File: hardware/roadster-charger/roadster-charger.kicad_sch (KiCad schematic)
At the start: 51 parts, among them J1 USB4505-03-0-A_REVA, J2 USB4505-03-0-A_REVA, J3 54-00166, Q1 CSD19532Q5B, U1 FUSB307BMPX, U10 OPA340NA, U2 ESP32-C3-MINI-1, U3 INA168, U4 LM5050-1, U5 INA168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

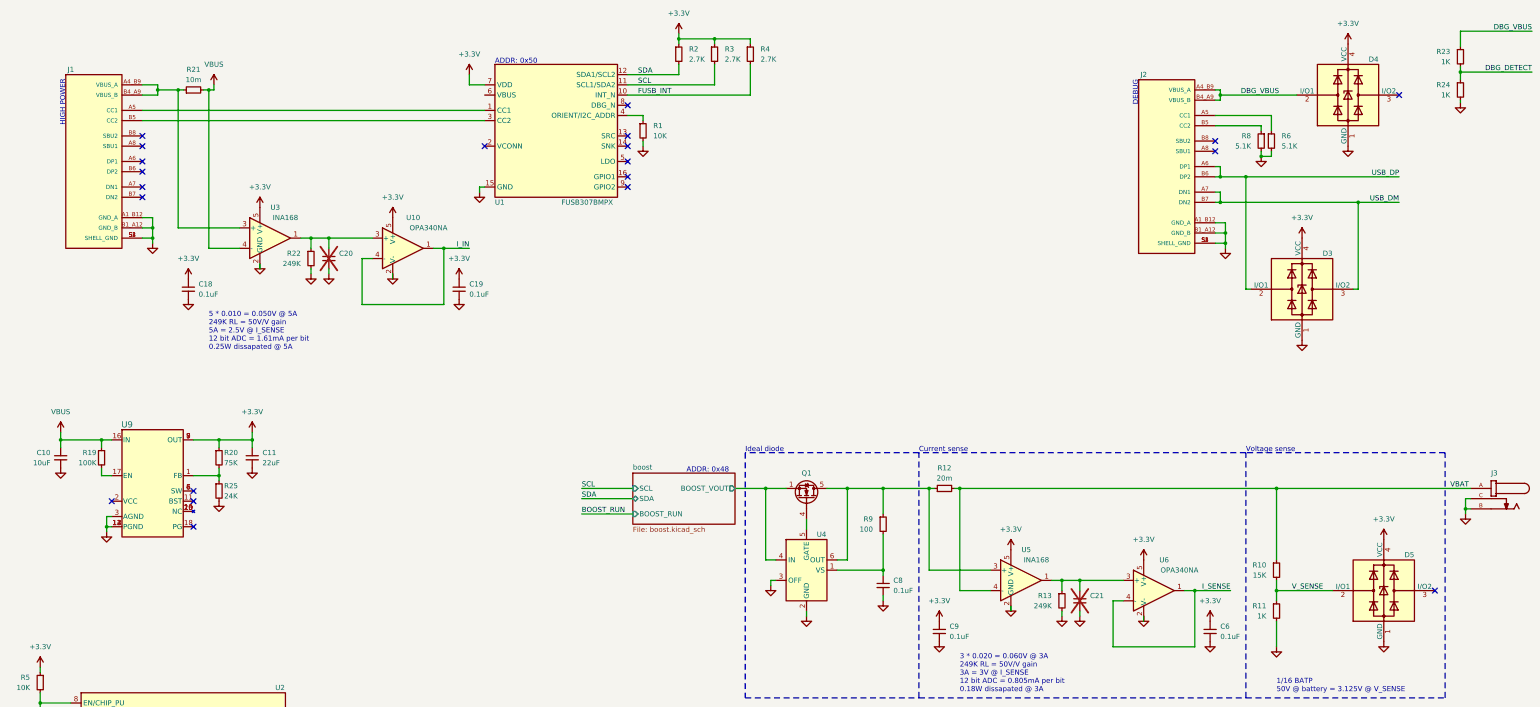
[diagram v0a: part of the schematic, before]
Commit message: fix accidental schem. grid change, add footprints and MPNs
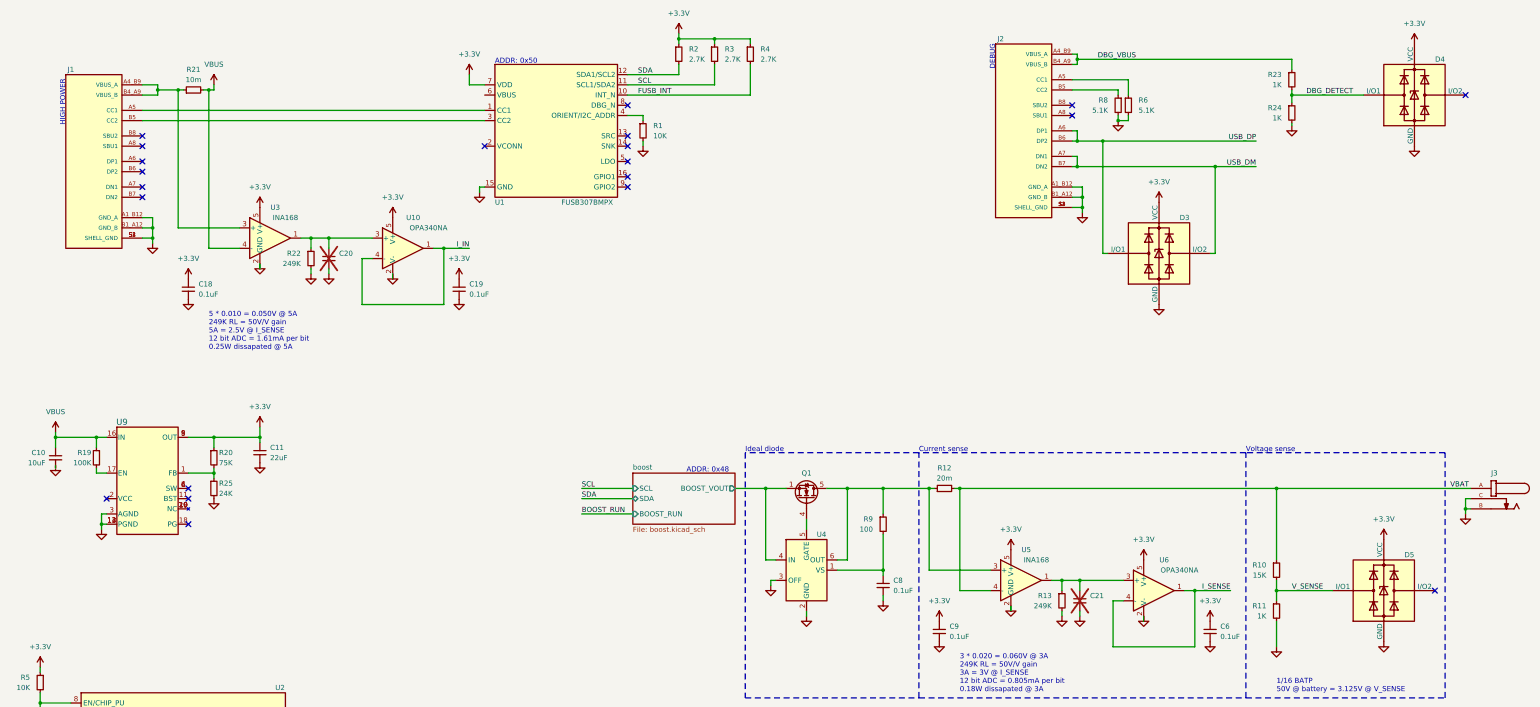
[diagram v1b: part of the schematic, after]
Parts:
- C1, C10: footprint (none) -> Capacitor_SMD:C_1206_3216Metric; MPN (none) -> CL31A106MBHNNNE
- C11: footprint (none) -> Capacitor_SMD:C_1206_3216Metric; MPN (none) -> CL31A226KAHNNNE
- C18, C19, C3, C4, C5, C6, C9: footprint (none) -> Capacitor_SMD:C_0603_1608Metric; MPN (none) -> CL10B104KB8NNNC
- C2: footprint (none) -> Capacitor_SMD:C_0805_2012Metric; MPN (none) -> CL21B105KAFNNNE
- C20, C21: footprint (none) -> Capacitor_SMD:C_0603_1608Metric; MPN (none) -> DNP
- C8: footprint (none) -> Capacitor_SMD:C_0603_1608Metric; MPN (none) -> CL10B104KC8NNNC
- D1, D2: MPN (none) -> COM-16347
- D3, D4, D5: MPN (none) -> PRTR5V0U2X,215
- J1, J2: value USB4505-03-0-A_REVA -> USB4505-03-0-A; footprint GCT_USB4505-03-0-A_REVA -> USB4505-03-0-A_REVA:GCT_USB4505-03-0-A_REVA; MANUFACTURER GCT -> (none); MAXIMUM_PACKAGE_HEIGHT 2.46mm -> (none); MPN (none) -> USB4505-03-0-A; PARTREV A -> (none); STANDARD Manufacturer Recommendations -> (none)
- J3: Availability In Stock -> (none); Check_prices https://www.snapeda.com/parts/54-00166/Tensility+Internatio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 -> (none); MANUFACTURER TENSILITY -> (none); MAXIMUM_PACKAGE_HEIGHT 11.2mm -> (none); MF Tensility International Corp -> (none); MP 54-00166 -> (none); MPN (none) -> 54-00166; PARTREV A -> (none); Purchase-URL https://www.snapeda.com/api/url_track_click_mouser/?unipart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 -> (none); SNAPEDA_PN 54-00166 -> (none); STANDARD Manufacturer Recommendations -> (none); SnapEDA_Link https://www.snapeda.com/parts/54-00166/Tensility+Internatio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 -> (none)
- Q1: MPN (none) -> CSD19532Q5B
- R1, R5, R7: footprint (none) -> Resistor_SMD:R_0603_1608Metric; MPN (none) -> RMCF0603FT10K0
- R10: footprint (none) -> Resistor_SMD:R_0603_1608Metric; MPN (none) -> RC0603JR-0715KL
- R11, R23, R24: footprint (none) -> Resistor_SMD:R_0603_1608Metric; MPN (none) -> RC0603FR-071KL
- R12: footprint (none) -> Resistor_SMD:R_0603_1608Metric
- R13, R22: footprint (none) -> Resistor_SMD:R_0603_1608Metric; MPN (none) -> RMCF0603FT249K
- R19: footprint (none) -> Resistor_SMD:R_0603_1608Metric; MPN (none) -> RC0603FR-07100KL
- R2, R3, R4: footprint (none) -> Resistor_SMD:R_0603_1608Metric; MPN (none) -> RC0603JR-072K7L
- R20: footprint (none) -> Resistor_SMD:R_0603_1608Metric; MPN (none) -> RC0603FR-0775KL
- R21: footprint (none) -> Resistor_SMD:R_0603_1608Metric; MPN LVT06R0020HER -> LVT06R0100FER
- R25: footprint (none) -> Resistor_SMD:R_0603_1608Metric; MPN (none) -> RC0603FR-1024KL
- R6, R8: footprint (none) -> Resistor_SMD:R_0603_1608Metric; MPN (none) -> RC0603FR-075K1L
- R9: footprint (none) -> Resistor_SMD:R_0603_1608Metric; MPN (none) -> RMCF0603FT100R
- U1: MPN (none) -> FUSB307BMPX
- U10, U6: MPN (none) -> OPA340NA
- U2: footprint Espressif:ESP32-C3-MINI-1 -> PCM_Espressif:ESP32-C3-MINI-1; MPN (none) -> ESP32-C3-MINI-1-N4
- U3, U5: MPN (none) -> INA168NA
- U4: MPN (none) -> LM5050MKX-1/NOPB
- U9: footprint QFN3p0x5p0x1p6_MPM3606A_MNP -> MPM3606A:QFN3p0x5p0x1p6_MPM3606A_MNP; MPN (none) -> MPM3606AGQV-P
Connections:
- net DBG_DETECT: now also D4.2 (I/O1)
- net DBG_VBUS: no longer D4.2 (I/O1)
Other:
- moved on the sheet: C10, C11, J2, R19, R20, R23, R24, R25, R6, R8, U9

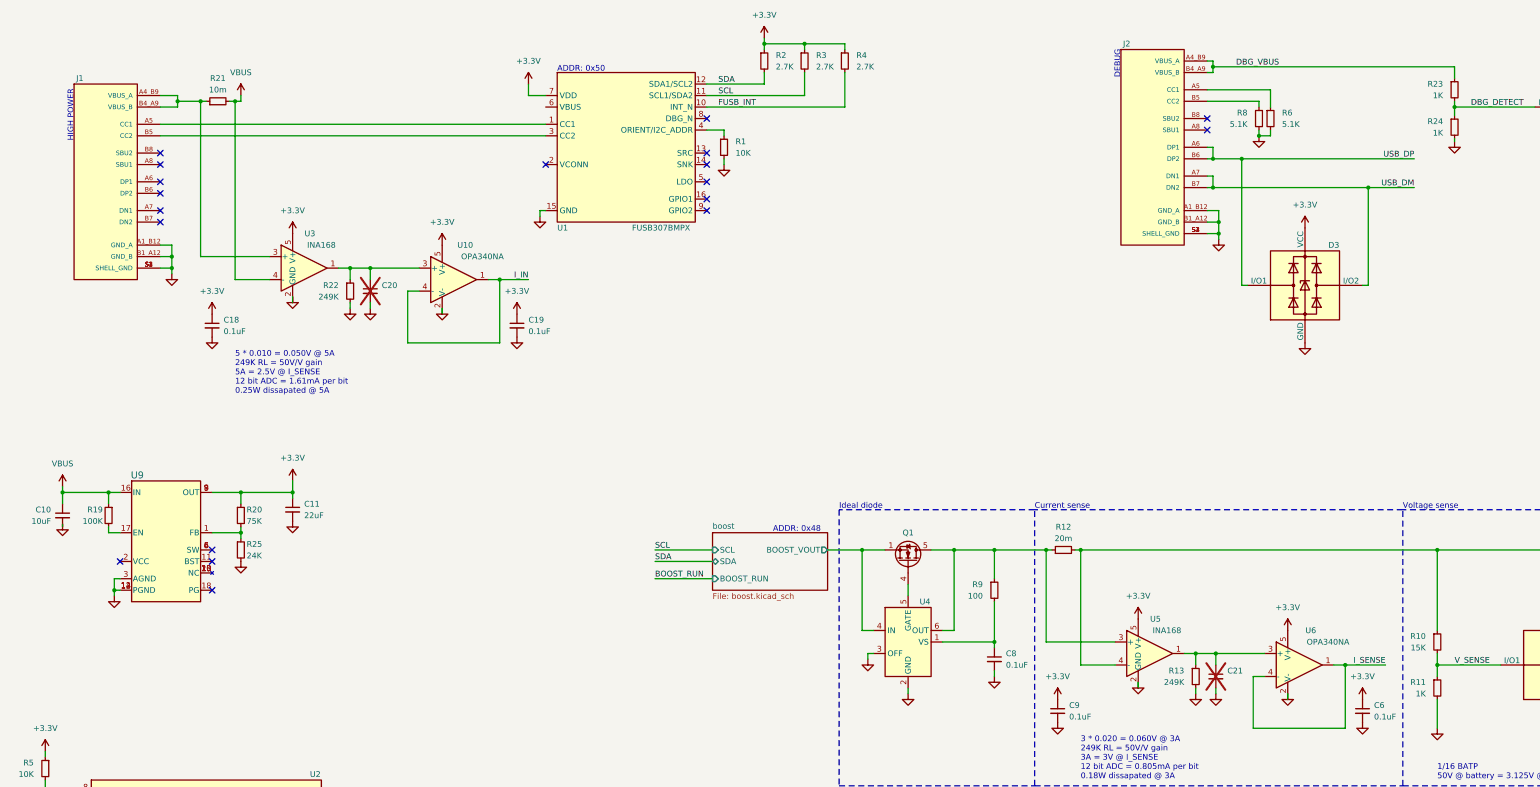
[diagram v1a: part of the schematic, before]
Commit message: edit ERC rules, clean up ERC errors, cleanup more off grid parts
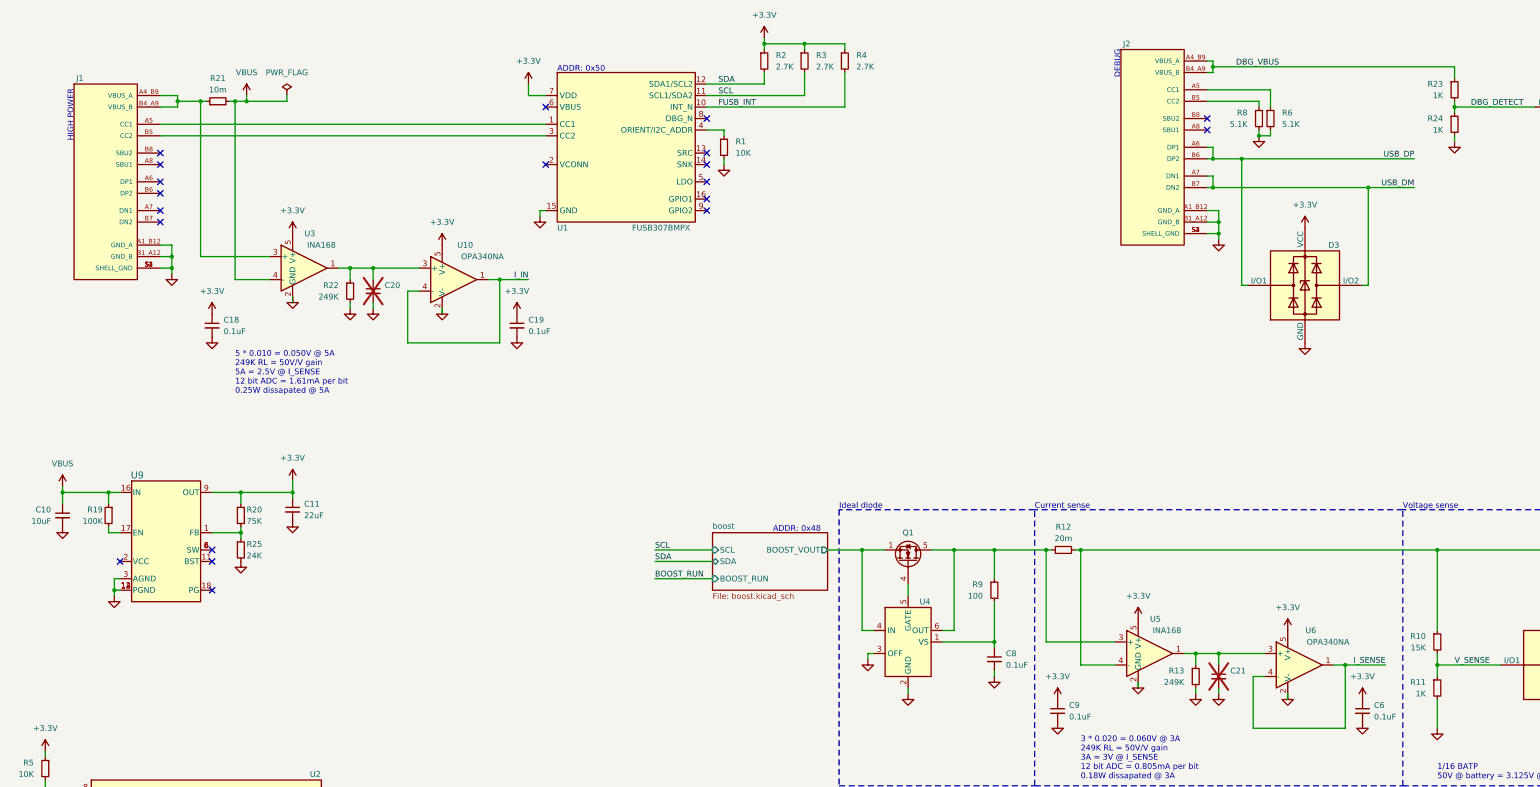
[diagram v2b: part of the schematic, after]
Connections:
- now unconnected: U9.10 (NC), U9.15 (NC), U9.19 (NC), U9.20 (NC)
- no-connect marks 24 -> 25
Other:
- moved on the sheet: C20, C21, R24

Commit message: wip routing
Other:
- note added: "CHANGE FB RESISTOR VALUES"
- note added: "TVS CLAMP"
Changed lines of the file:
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@@
     (effects (font (size 1.27 1.27)) (justify left bottom))
+  )
+  (text "TVS CLAMP" (at 210.82 181.61 0)
+    (effects (font (size 3 3) (thickness 0.6) bold (color 255 22 22 1)) (justify left bottom))
   )
   (text "1/16 BATP\n50V @ battery = 3.125V @ V_SENSE" (at 340.36 189.23 0)
@@
     (effects (font (size 1.27 1.27)) (justify left bottom))
   )
+  (text "CHANGE FB RESISTOR VALUES" (at 31.75 158.75 0)
+    (effects (font (size 3 3) (thickness 0.6) bold (color 255 22 22 1)) (justify left bottom))
+  )
   (label "V_SENSE" (at 344.17 163.83 0) (fields_autoplaced)

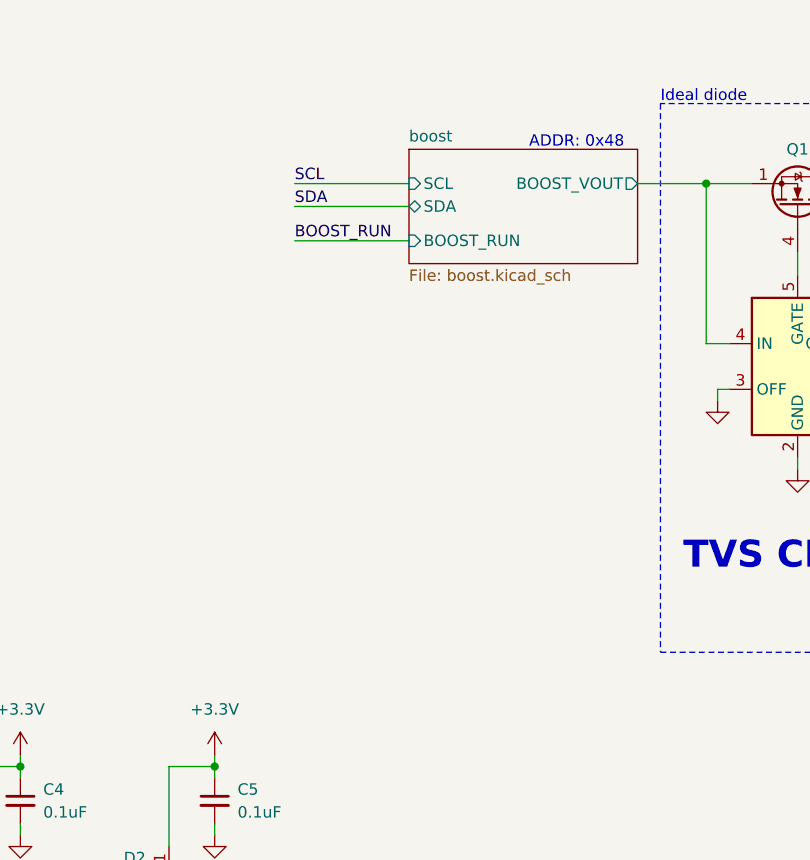
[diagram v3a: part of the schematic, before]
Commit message: add LM75 i2c current sensor
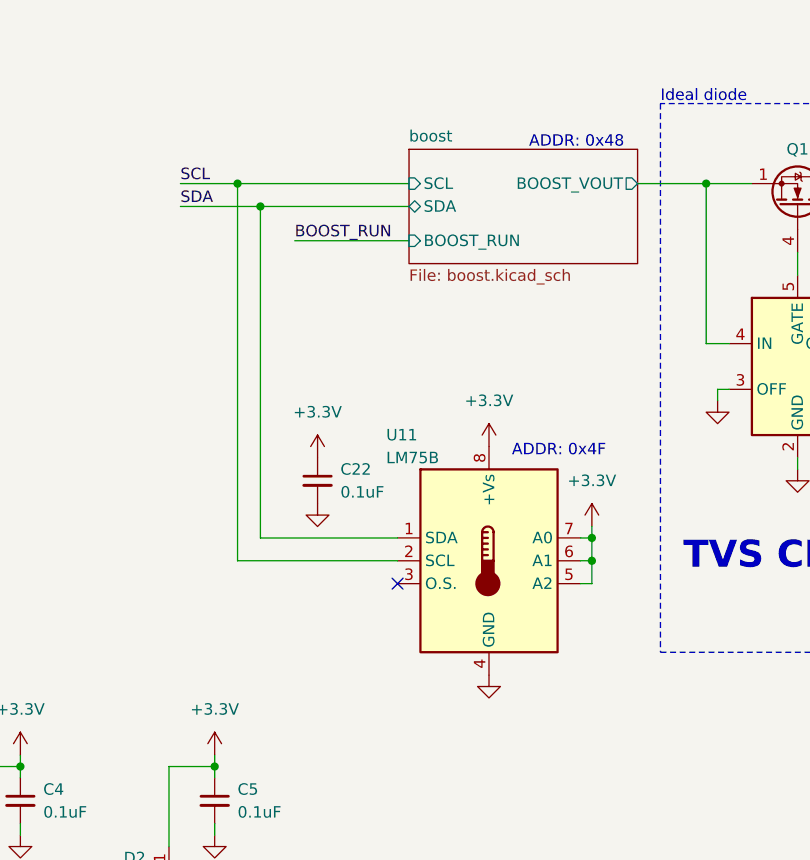
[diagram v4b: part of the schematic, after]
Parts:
- added C22: 0.1uF, Capacitor_SMD:C_0603_1608Metric, symbol Device:C_Small
- added U11: LM75B, Package_SO:SOIC-8_3.9x4.9mm_P1.27mm, symbol Sensor_Temperature:LM75B
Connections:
- net +3.3V: now also C22.1, U11.5 (A2), U11.6 (A1), U11.7 (A0), U11.8 (+Vs)
- net GND: now also C22.2, U11.4 (GND)
- net SCL: now also U11.2 (SCL)
- net SDA: now also U11.1 (SDA)
- no-connect marks 25 -> 26
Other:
- note added: "ADDR: 0x4F"

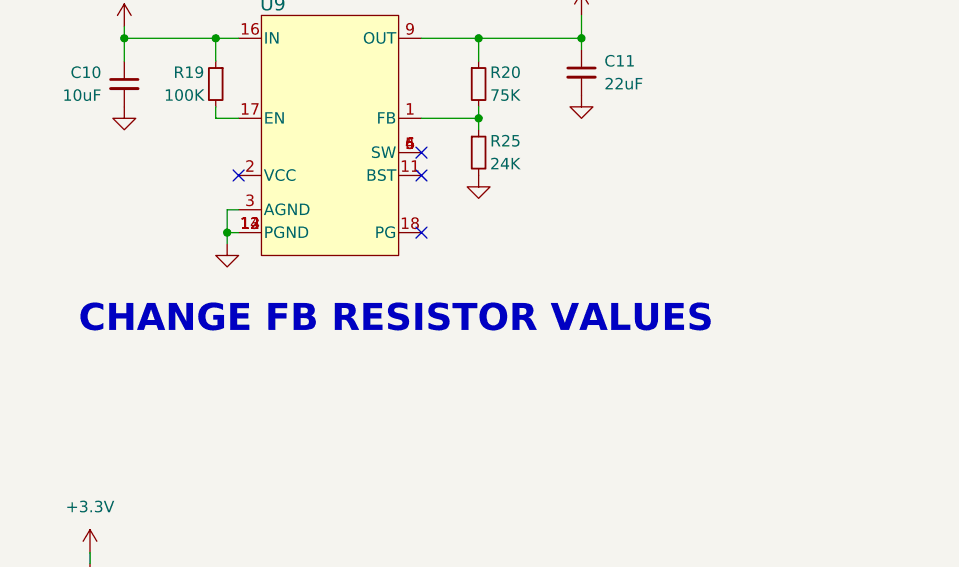
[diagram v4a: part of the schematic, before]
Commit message: add AAM resistor to 3V3 regulator, validate feedback resistors
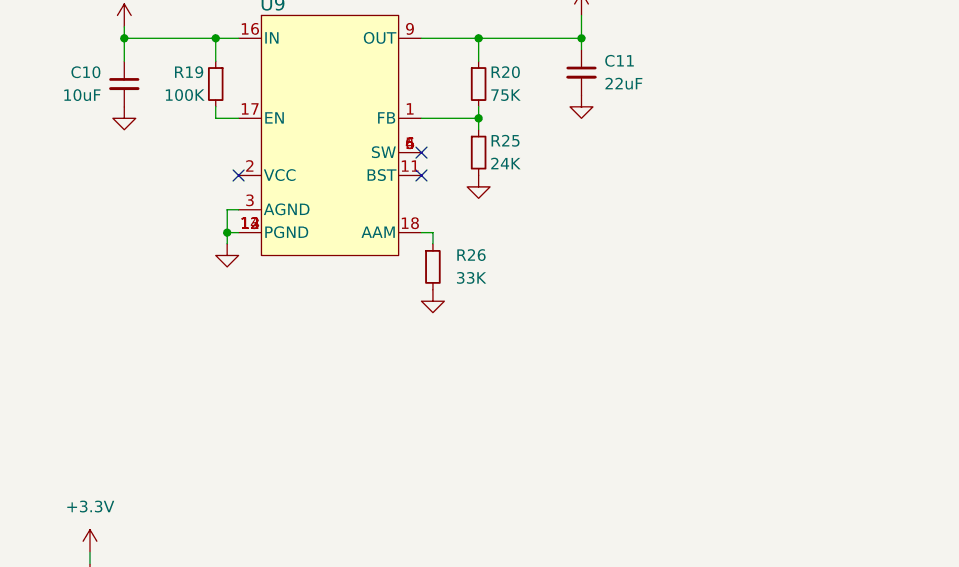
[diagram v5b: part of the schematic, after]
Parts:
- added R26: 33K, Resistor_SMD:R_0603_1608Metric, symbol Device:R_Small
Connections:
- net GND: now also R26.2
- net at U9.18 (AAM): now also R26.1
- no-connect marks 26 -> 25
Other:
- note removed: "CHANGE FB RESISTOR VALUES"
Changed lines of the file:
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@@
   (no_connect (at 289.56 43.18))
   (no_connect (at 69.85 140.97))
-  (no_connect (at 69.85 147.32))
   (no_connect (at 289.56 45.72))
   (no_connect (at 161.29 219.71))
@@
     (stroke (width 0) (type default))
   )
+  (wire (pts (xy 69.85 147.32) (xy 71.12 147.32))
+    (stroke (width 0) (type default))
+  )
   (polyline (pts (xy 208.28 190.5) (xy 251.46 190.5))
     (stroke (width 0) (type dash))
@@
     (stroke (width 0) (type default))
   )
+  (wire (pts (xy 71.12 147.32) (xy 71.12 148.59))
+    (stroke (width 0) (type default))
+  )
   (wire (pts (xy 96.52 207.01) (xy 109.22 207.01))
     (stroke (width 0) (type default))
@@
     (effects (font (size 1.27 1.27)) (justify left bottom))
   )
-  (text "CHANGE FB RESISTOR VALUES" (at 31.75 158.75 0)
-    (effects (font (size 3 3) (thickness 0.6) bold (color 255 22 22 1)) (justify left bottom))
-  )
   (label "V_SENSE" (at 344.17 163.83 0) (fields_autoplaced)
     (effects (font (size 1.27 1.27)) (justify left bottom))
@@
     )
   )
+  (symbol (lib_id "Device:R_Small") (at 71.12 151.13 0) (unit 1)
+    (in_bom yes) (on_board yes) (dnp no)
+    (property "Reference" "R26" (at 73.66 149.86 0)
+      (effects (font (size 1.27 1.27)) (justify left))
+    )
+    (property "Value" "33K" (at 73.66 152.4 0)
+      (effects (font (size 1.27 1.27)) (justify left))
+    )
+    (property "Footprint" "Resistor_SMD:R_0603_1608Metric" (at 71.12 151.13 0)
+      (effects (font (size 1.27 1.27)) hide)
+    )
+    (property "Datasheet" "~" (at 71.12 151.13 0)
+      (effects (font (size 1.27 1.27)) hide)
+    )
+    (property "MPN" "RMCF0603FT33K0" (at 71.12 151.13 0)
+      (effects (font (size 1.27 1.27)) hide)
+    )
+    (pin "1")
+    (pin "2")
+    (instances
+      (project "roadster-charger"
+        (path "/57ecac41-cd8a-4182-a81e-fed3e381aedd"
+          (reference "R26") (unit 1)
+        )
+      )
+    )
+  )
   (symbol (lib_id "power:GND") (at 182.88 53.34 0) (unit 1)
     (in_bom yes) (on_board yes) (dnp no)
@@
         )
       )
+    )
+  )
+  (symbol (lib_id "power:GND") (at 71.12 153.67 0) (unit 1)
+    (in_bom yes) (on_board yes) (dnp no)
+    (property "Reference" "#PWR078" (at 71.12 160.02 0)
+      (effects (font (size 1.27 1.27)) hide)
+    )
+    (property "Value" "GND" (at 71.12 158.75 0)
+      (effects (font (size 1.27 1.27)) hide)
+    )
+    (property "Footprint" "" (at 71.12 153.67 0)
+      (effects (font (size 1.27 1.27)) hide)
+    )
+    (property "Datasheet" "" (at 71.12 153.67 0)
+      (effects (font (size 1.27 1.27)) hide)
+    )
+    (pin "1")
+    (instances
+      (project "roadster-charger"
+        (path "/57ecac41-cd8a-4182-a81e-fed3e381aedd"
+          (reference "#PWR078") (unit 1)
+        )
+      )
